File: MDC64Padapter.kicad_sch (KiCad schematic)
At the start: 36 parts, among them J1 DB9_F_TO_C64, J2 DB9_M_TO_PAD, Q1 BC847, Q2 BC847, SW1 MODE, U1 74ACT08, U2 74ACT373, U3 74ACT157, U4 74ACT373, U5 74AHC1G04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

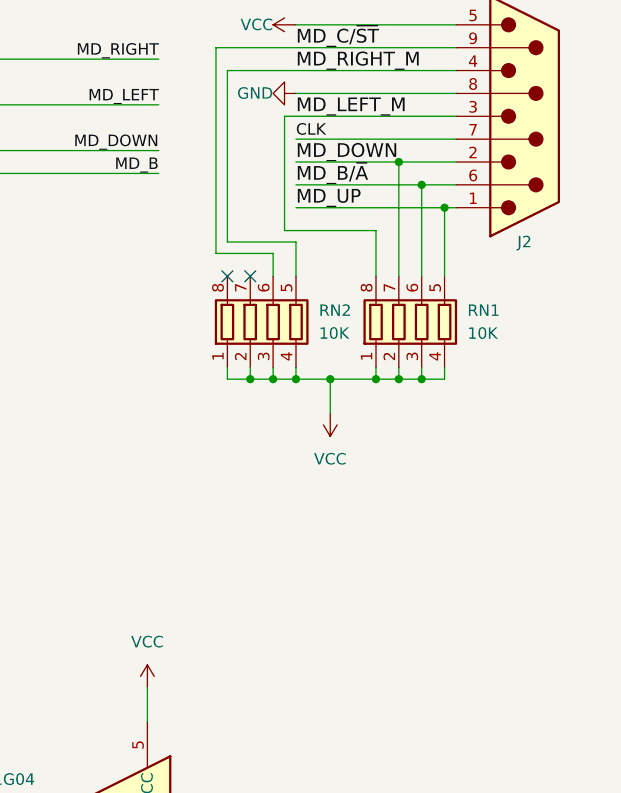
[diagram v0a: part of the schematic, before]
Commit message: Add filter caps on up/down direction
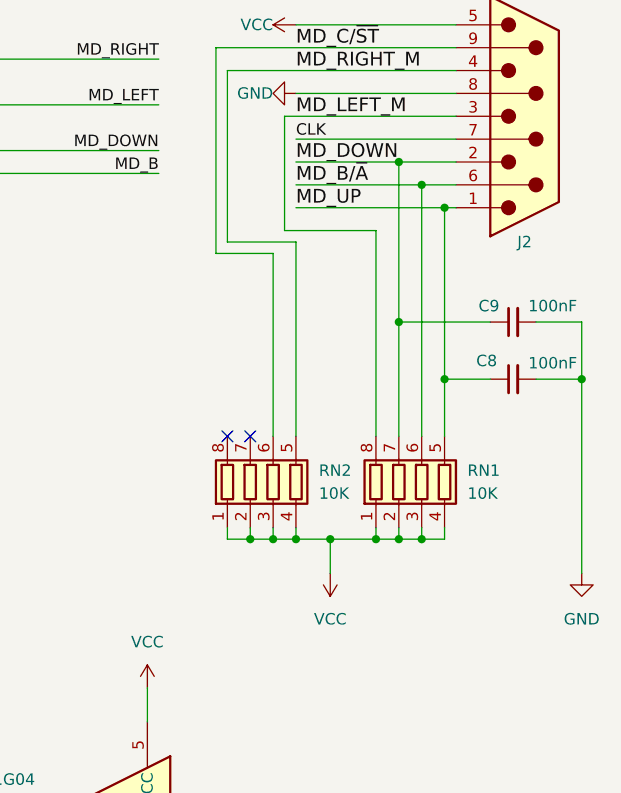
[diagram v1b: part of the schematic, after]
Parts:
- added C8, C9: 100nF, Capacitor_SMD:C_1206_3216Metric_Pad1.33x1.80mm_HandSolder, symbol Device:C_Small
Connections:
- net C64_DOWN: now also C9.1
- net GND: now also C8.2, C9.2
- net MD_UP: now also C8.1
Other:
- moved on the sheet: RN1, RN2

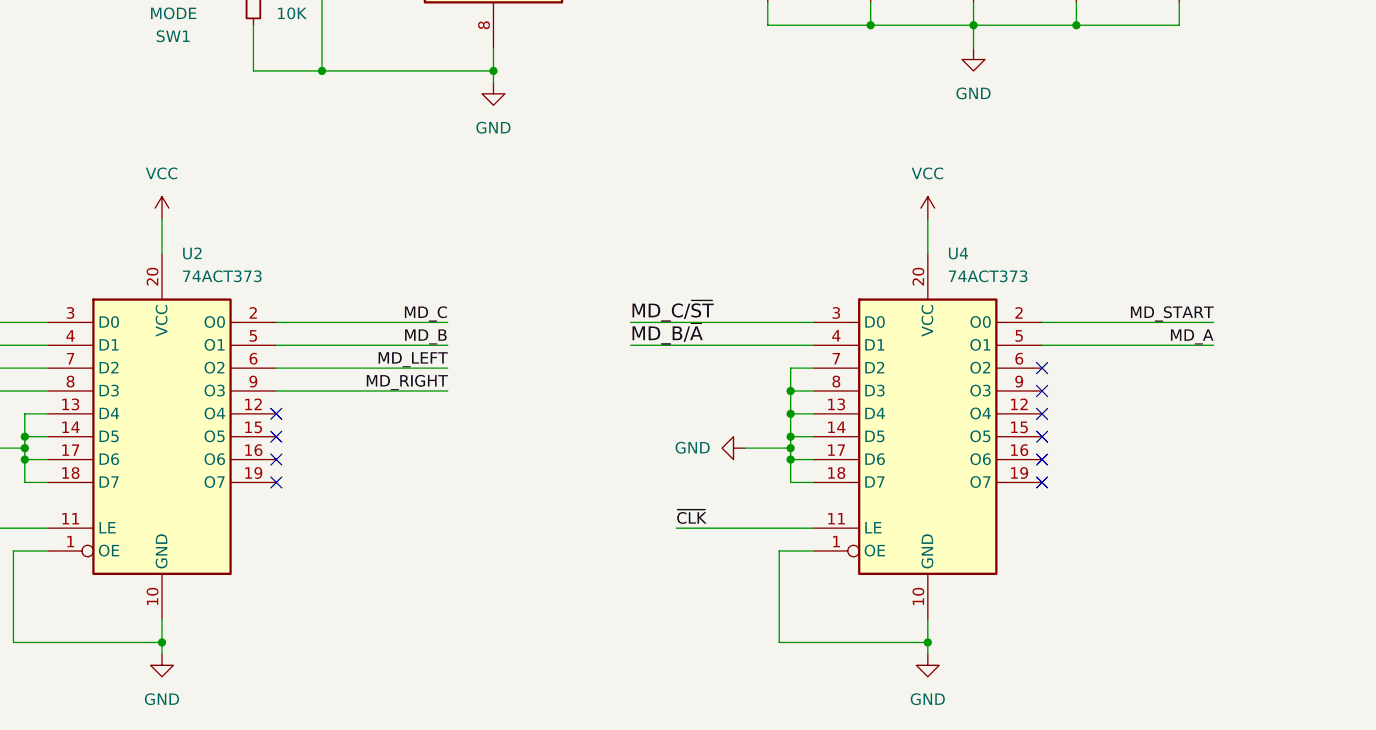
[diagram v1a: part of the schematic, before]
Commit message: Add filtering caps to the outputs of the latches
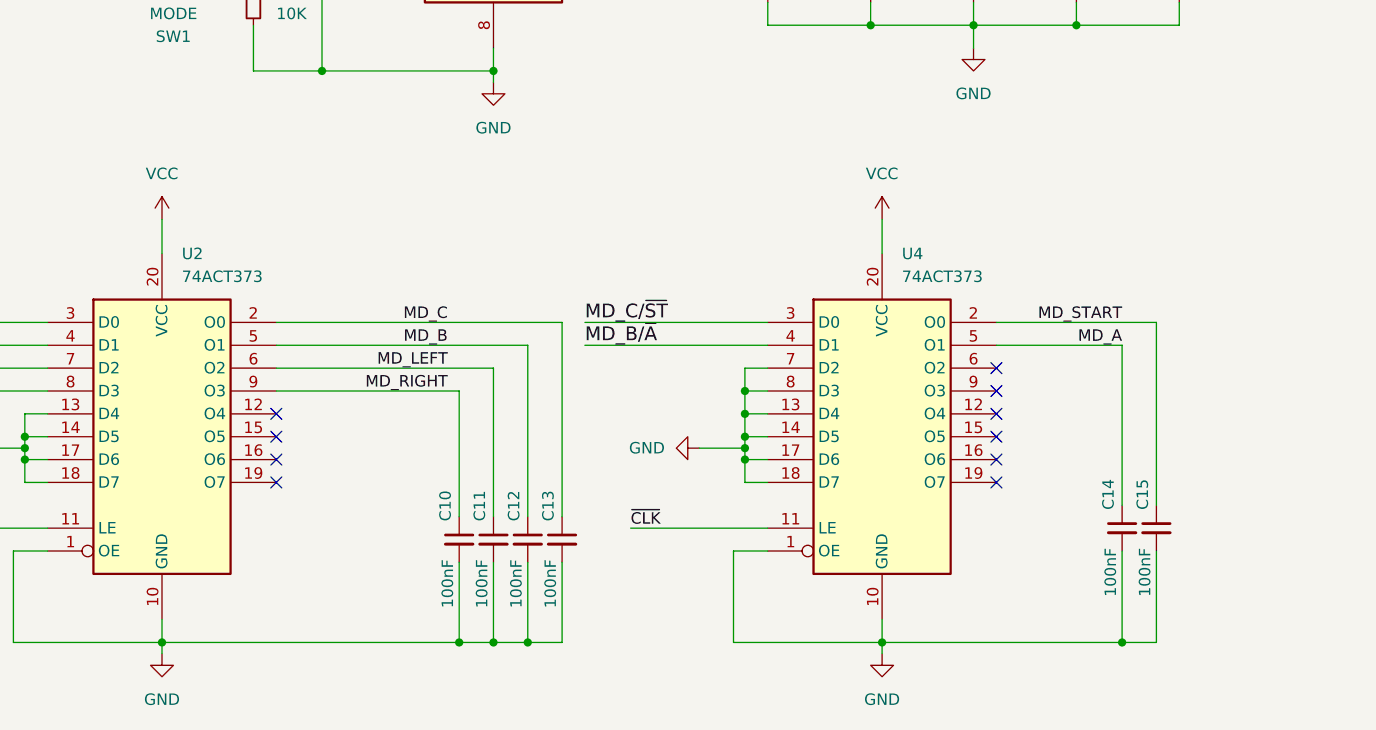
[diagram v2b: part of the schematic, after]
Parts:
- added C10, C11, C12, C13, C14, C15: 100nF, Capacitor_SMD:C_1206_3216Metric_Pad1.33x1.80mm_HandSolder, symbol Device:C_Small
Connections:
- net C64_FIRE: now also C12.1
- net C64_LEFT: now also C11.1
- net C64_RIGHT: now also C10.1
- net GND: now also C10.2, C11.2, C12.2, C13.2, C14.2, C15.2
- net MD_A: now also C14.1
- net MD_C: now also C13.1
- net MD_START: now also C15.1
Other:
- moved on the sheet: U4

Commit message: Begin reorganizing the board
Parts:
- C1, C10, C11, C12, C13, C14, C15, C2, C3, C4, C5, C6, C7, C8, C9: footprint Capacitor_SMD:C_1206_3216Metric_Pad1.33x1.80mm_HandSolder -> Capacitor_SMD:C_0805_2012Metric_Pad1.18x1.45mm_HandSolder
- JP1, JP2: footprint Jumper:SolderJumper-3_P1.3mm_Open_RoundedPad1.0x1.5mm -> Connector_PinHeader_2.54mm:PinHeader_1x03_P2.54mm_Horizontal
- R1, R2, R3, R4, R5, R6, R7, R8, R9: footprint Resistor_SMD:R_1206_3216Metric_Pad1.30x1.75mm_HandSolder -> Resistor_SMD:R_0805_2012Metric_Pad1.20x1.40mm_HandSolder
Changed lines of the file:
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@@
 			)
 		)
-		(property "Footprint" "Capacitor_SMD:C_1206_3216Metric_Pad1.33x1.80mm_HandSolder"
+		(property "Footprint" "Capacitor_SMD:C_0805_2012Metric_Pad1.18x1.45mm_HandSolder"
 			(at 209.55 139.7 0)
 			(effects
@@
 			)
 		)
-		(property "Footprint" "Capacitor_SMD:C_1206_3216Metric_Pad1.33x1.80mm_HandSolder"
+		(property "Footprint" "Capacitor_SMD:C_0805_2012Metric_Pad1.18x1.45mm_HandSolder"
 			(at 173.99 171.45 0)
 			(effects
@@
 			)
 		)
-		(property "Footprint" "Capacitor_SMD:C_1206_3216Metric_Pad1.33x1.80mm_HandSolder"
+		(property "Footprint" "Capacitor_SMD:C_0805_2012Metric_Pad1.18x1.45mm_HandSolder"
 			(at 142.24 110.49 0)
 			(effects
@@
 			)
 		)
-		(property "Footprint" "Capacitor_SMD:C_1206_3216Metric_Pad1.33x1.80mm_HandSolder"
+		(property "Footprint" "Capacitor_SMD:C_0805_2012Metric_Pad1.18x1.45mm_HandSolder"
 			(at 100.33 172.72 0)
 			(effects
@@
 			)
 		)
-		(property "Footprint" "Capacitor_SMD:C_1206_3216Metric_Pad1.33x1.80mm_HandSolder"
+		(property "Footprint" "Capacitor_SMD:C_0805_2012Metric_Pad1.18x1.45mm_HandSolder"
 			(at 104.14 172.72 0)
 			(effects
@@
 			)
 		)
-		(property "Footprint" "Capacitor_SMD:C_1206_3216Metric_Pad1.33x1.80mm_HandSolder"
+		(property "Footprint" "Capacitor_SMD:C_0805_2012Metric_Pad1.18x1.45mm_HandSolder"
 			(at 170.18 171.45 0)
 			(effects
@@
 			)
 		)
-		(property "Footprint" "Jumper:SolderJumper-3_P1.3mm_Open_RoundedPad1.0x1.5mm"
+		(property "Footprint" "Connector_PinHeader_2.54mm:PinHeader_1x03_P2.54mm_Horizontal"
 			(at 87.63 48.26 0)
 			(effects
@@
 			)
 		)
-		(property "Footprint" "Resistor_SMD:R_1206_3216Metric_Pad1.30x1.75mm_HandSolder"
+		(property "Footprint" "Resistor_SMD:R_0805_2012Metric_Pad1.20x1.40mm_HandSolder"
 			(at 73.66 113.03 0)
 			(effects
@@
 			)
 		)
-		(property "Footprint" "Capacitor_SMD:C_1206_3216Metric_Pad1.33x1.80mm_HandSolder"
+		(property "Footprint" "Capacitor_SMD:C_0805_2012Metric_Pad1.18x1.45mm_HandSolder"
 			(at 107.95 172.72 0)
 			(effects
@@
 			)
 		)
-		(property "Footprint" "Resistor_SMD:R_1206_3216Metric_Pad1.30x1.75mm_HandSolder"
+		(property "Footprint" "Resistor_SMD:R_0805_2012Metric_Pad1.20x1.40mm_HandSolder"
 			(at 271.78 142.24 0)
 			(effects
@@
 			)
 		)
-		(property "Footprint" "Capacitor_SMD:C_1206_3216Metric_Pad1.33x1.80mm_HandSolder"
+		(property "Footprint" "Capacitor_SMD:C_0805_2012Metric_Pad1.18x1.45mm_HandSolder"
 			(at 153.67 110.49 0)
 			(effects
@@
 			)
 		)
-		(property "Footprint" "Resistor_SMD:R_1206_3216Metric_Pad1.30x1.75mm_HandSolder"
+		(property "Footprint" "Resistor_SMD:R_0805_2012Metric_Pad1.20x1.40mm_HandSolder"
 			(at 29.972 25.4 90)
 			(effects
@@
 			)
 		)
-		(property "Footprint" "Capacitor_SMD:C_1206_3216Metric_Pad1.33x1.80mm_HandSolder"
+		(property "Footprint" "Capacitor_SMD:C_0805_2012Metric_Pad1.18x1.45mm_HandSolder"
 			(at 273.05 54.61 0)
 			(effects
@@
 			)
 		)
-		(property "Footprint" "Resistor_SMD:R_1206_3216Metric_Pad1.30x1.75mm_HandSolder"
+		(property "Footprint" "Resistor_SMD:R_0805_2012Metric_Pad1.20x1.40mm_HandSolder"
 			(at 40.64 28.702 90)
 			(effects
@@
 			)
 		)
-		(property "Footprint" "Resistor_SMD:R_1206_3216Metric_Pad1.30x1.75mm_HandSolder"
+		(property "Footprint" "Resistor_SMD:R_0805_2012Metric_Pad1.20x1.40mm_HandSolder"
 			(at 98.552 25.4 90)
 			(effects
@@
 			)
 		)
-		(property "Footprint" "Resistor_SMD:R_1206_3216Metric_Pad1.30x1.75mm_HandSolder"
+		(property "Footprint" "Resistor_SMD:R_0805_2012Metric_Pad1.20x1.40mm_HandSolder"
 			(at 109.22 28.702 90)
 			(effects
@@
 			)
 		)
-		(property "Footprint" "Capacitor_SMD:C_1206_3216Metric_Pad1.33x1.80mm_HandSolder"
+		(property "Footprint" "Capacitor_SMD:C_0805_2012Metric_Pad1.18x1.45mm_HandSolder"
 			(at 130.81 110.49 0)
 			(effects
@@
 			)
 		)
-		(property "Footprint" "Capacitor_SMD:C_1206_3216Metric_Pad1.33x1.80mm_HandSolder"
+		(property "Footprint" "Capacitor_SMD:C_0805_2012Metric_Pad1.18x1.45mm_HandSolder"
 			(at 227.33 137.16 0)
 			(effects
@@
 			)
 		)
-		(property "Footprint" "Capacitor_SMD:C_1206_3216Metric_Pad1.33x1.80mm_HandSolder"
+		(property "Footprint" "Capacitor_SMD:C_0805_2012Metric_Pad1.18x1.45mm_HandSolder"
 			(at 273.05 60.96 0)
 			(effects
@@
 			)
 		)
-		(property "Footprint" "Capacitor_SMD:C_1206_3216Metric_Pad1.33x1.80mm_HandSolder"
+		(property "Footprint" "Capacitor_SMD:C_0805_2012Metric_Pad1.18x1.45mm_HandSolder"
 			(at 176.53 110.49 0)
 			(effects
@@
 			)
 		)
-		(property "Footprint" "Jumper:SolderJumper-3_P1.3mm_Open_RoundedPad1.0x1.5mm"
+		(property "Footprint" "Connector_PinHeader_2.54mm:PinHeader_1x03_P2.54mm_Horizontal"
 			(at 21.59 48.26 0)
 			(effects
@@
 			)
 		)
-		(property "Footprint" "Resistor_SMD:R_1206_3216Metric_Pad1.30x1.75mm_HandSolder"
+		(property "Footprint" "Resistor_SMD:R_0805_2012Metric_Pad1.20x1.40mm_HandSolder"
 			(at 276.86 132.08 0)
 			(effects
@@
 			)
 		)
-		(property "Footprint" "Resistor_SMD:R_1206_3216Metric_Pad1.30x1.75mm_HandSolder"
+		(property "Footprint" "Resistor_SMD:R_0805_2012Metric_Pad1.20x1.40mm_HandSolder"
 			(at 57.15 36.322 90)
 			(effects
@@
 			)
 		)
-		(property "Footprint" "Capacitor_SMD:C_1206_3216Metric_Pad1.33x1.80mm_HandSolder"
+		(property "Footprint" "Capacitor_SMD:C_0805_2012Metric_Pad1.18x1.45mm_HandSolder"
 			(at 165.1 110.49 0)
 			(effects
@@
 			)
 		)
-		(property "Footprint" "Resistor_SMD:R_1206_3216Metric_Pad1.30x1.75mm_HandSolder"
+		(property "Footprint" "Resistor_SMD:R_0805_2012Metric_Pad1.20x1.40mm_HandSolder"
 			(at 125.73 36.322 90)
 			(effects
@@
 			)
 		)
-		(property "Footprint" "Capacitor_SMD:C_1206_3216Metric_Pad1.33x1.80mm_HandSolder"
+		(property "Footprint" "Capacitor_SMD:C_0805_2012Metric_Pad1.18x1.45mm_HandSolder"
 			(at 96.52 172.72 0)
 			(effects

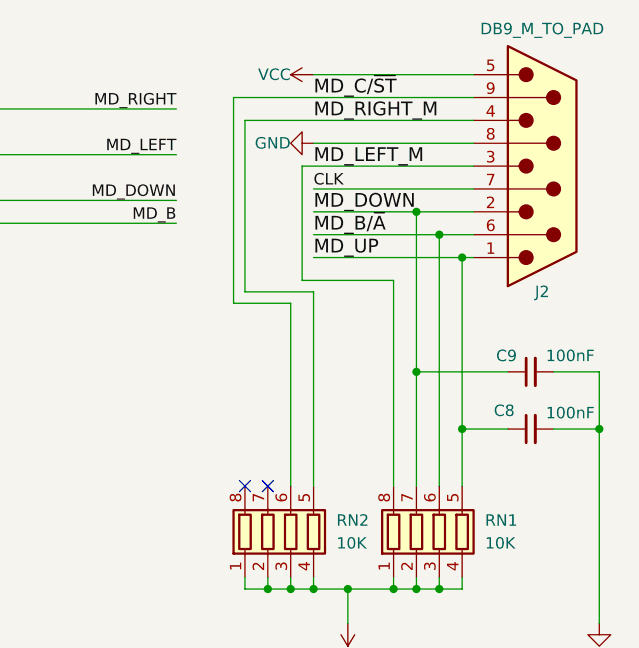
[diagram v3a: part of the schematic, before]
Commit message: Reroute the adapter
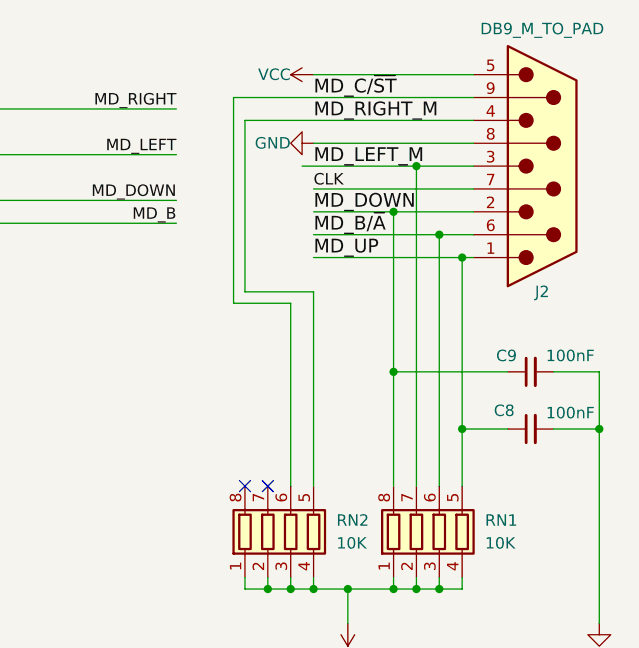
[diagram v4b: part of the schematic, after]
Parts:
- JP1, JP2: footprint Connector_PinHeader_2.54mm:PinHeader_1x03_P2.54mm_Horizontal -> Connector_PinHeader_2.54mm:PinHeader_1x03_P2.54mm_Vertical
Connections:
- net C64_DOWN: now also RN1.8 (R1.2); no longer RN1.7 (R2.2)
- net MD_LEFT_M: now also RN1.7 (R2.2); no longer RN1.8 (R1.2)
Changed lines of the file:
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@@
 	)
 	(junction
+		(at 257.81 36.83)
+		(diameter 0)
+		(color 0 0 0 0)
+	)
+	(junction
 		(at 260.35 78.74)
 		(diameter 0)
@@
 	)
 	(junction
-		(at 260.35 54.61)
+		(at 165.1 115.57)
 		(diameter 0)
 		(color 0 0 0 0)
 	)
 	(junction
-		(at 165.1 115.57)
+		(at 257.81 54.61)
 		(diameter 0)
 		(color 0 0 0 0)
@@
 	)
 	(junction
-		(at 260.35 36.83)
-		(diameter 0)
-		(color 0 0 0 0)
-	)
-	(junction
 		(at 128.27 156.21)
 		(diameter 0)
@@
 	)
 	(junction
+		(at 260.35 31.75)
+		(diameter 0)
+		(color 0 0 0 0)
+	)
+	(junction
 		(at 170.18 184.15)
 		(diameter 0)
@@
 	(wire
 		(pts
+			(xy 257.81 54.61) (xy 257.81 67.31)
+		)
+		(stroke
+			(width 0)
+			(type default)
+		)
+	)
+	(wire
+		(pts
 			(xy 240.03 24.13) (xy 240.03 46.99)
 		)
@@
 	(wire
 		(pts
-			(xy 260.35 36.83) (xy 266.7 36.83)
+			(xy 248.92 36.83) (xy 257.81 36.83)
 		)
 		(stroke
@@
 	(wire
 		(pts
+			(xy 257.81 36.83) (xy 257.81 54.61)
+		)
+		(stroke
+			(width 0)
+			(type default)
+		)
+	)
+	(wire
+		(pts
 			(xy 128.27 162.56) (xy 128.27 163.83)
 		)
@@
 	(wire
 		(pts
-			(xy 248.92 36.83) (xy 260.35 36.83)
-		)
-		(stroke
-			(width 0)
-			(type default)
-		)
-	)
-	(wire
-		(pts
 			(xy 128.27 153.67) (xy 128.27 156.21)
 		)
@@
 	(wire
 		(pts
-			(xy 260.35 36.83) (xy 260.35 54.61)
-		)
-		(stroke
-			(width 0)
-			(type default)
-		)
-	)
-	(wire
-		(pts
 			(xy 48.26 163.83) (xy 48.26 166.37)
 		)
@@
 	(wire
 		(pts
-			(xy 257.81 44.45) (xy 257.81 67.31)
-		)
-		(stroke
-			(width 0)
-			(type default)
-		)
-	)
-	(wire
-		(pts
 			(xy 100.33 29.21) (xy 100.33 30.48)
 		)
@@
 	(wire
 		(pts
-			(xy 247.65 31.75) (xy 266.7 31.75)
+			(xy 247.65 31.75) (xy 260.35 31.75)
 		)
 		(stroke
@@
 	(wire
 		(pts
-			(xy 260.35 54.61) (xy 260.35 67.31)
+			(xy 260.35 31.75) (xy 260.35 67.31)
 		)
 		(stroke
@@
 	(wire
 		(pts
-			(xy 247.65 44.45) (xy 247.65 31.75)
+			(xy 19.05 90.17) (xy 30.48 90.17)
 		)
 		(stroke
@@
 	(wire
 		(pts
-			(xy 19.05 90.17) (xy 30.48 90.17)
+			(xy 257.81 54.61) (xy 270.51 54.61)
 		)
 		(stroke
@@
 	(wire
 		(pts
-			(xy 257.81 44.45) (xy 247.65 44.45)
-		)
-		(stroke
-			(width 0)
-			(type default)
-		)
-	)
-	(wire
-		(pts
 			(xy 15.24 30.48) (xy 15.24 48.26)
 		)
@@
 	(wire
 		(pts
+			(xy 257.81 36.83) (xy 266.7 36.83)
+		)
+		(stroke
+			(width 0)
+			(type default)
+		)
+	)
+	(wire
+		(pts
 			(xy 66.04 80.01) (xy 87.63 80.01)
 		)
@@
 	(wire
 		(pts
-			(xy 170.18 168.91) (xy 170.18 151.13)
+			(xy 260.35 31.75) (xy 266.7 31.75)
 		)
 		(stroke
@@
 	(wire
 		(pts
-			(xy 76.2 156.21) (xy 96.52 156.21)
+			(xy 170.18 168.91) (xy 170.18 151.13)
 		)
 		(stroke
@@
 	(wire
 		(pts
-			(xy 48.26 163.83) (xy 50.8 163.83)
+			(xy 76.2 156.21) (xy 96.52 156.21)
 		)
 		(stroke
@@
 	(wire
 		(pts
-			(xy 100.33 118.11) (xy 100.33 120.65)
+			(xy 48.26 163.83) (xy 50.8 163.83)
 		)
 		(stroke
@@
 	(wire
 		(pts
-			(xy 31.75 29.21) (xy 31.75 30.48)
+			(xy 100.33 118.11) (xy 100.33 120.65)
 		)
 		(stroke
@@
 	(wire
 		(pts
-			(xy 260.35 54.61) (xy 270.51 54.61)
+			(xy 31.75 29.21) (xy 31.75 30.48)
 		)
 		(stroke
@@
 			)
 		)
-		(property "Footprint" "Connector_PinHeader_2.54mm:PinHeader_1x03_P2.54mm_Horizontal"
+		(property "Footprint" "Connector_PinHeader_2.54mm:PinHeader_1x03_P2.54mm_Vertical"
 			(at 87.63 48.26 0)
 			(effects
@@
 			)
 		)
-		(property "Footprint" "Connector_PinHeader_2.54mm:PinHeader_1x03_P2.54mm_Horizontal"
+		(property "Footprint" "Connector_PinHeader_2.54mm:PinHeader_1x03_P2.54mm_Vertical"
 			(at 21.59 48.26 0)
 			(effects
